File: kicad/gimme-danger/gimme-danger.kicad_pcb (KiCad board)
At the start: 4 copper layers, 46.1 x 30 mm, 74 parts, among them J3 Screw_Terminal_01x06, Q1 AO3400A, Q2 AO3400A, Q3 AO3400A, Q4 AO3400A, U1 ESP32-S3-WROOM-1, U2 TPD6S300RUKR, U3 U261-241N-4BS2SS, U4 AO4407A, U5 SKRKAEE020, U6 DDTC143EUA, U7 SKRKAEE020, U8 TPS54302

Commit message: v0.0.2a routing v0
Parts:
- removed C13: 0.1u, Capacitor_SMD:C_0402_1005Metric
- removed R1, R7: 10k, Resistor_SMD:R_0402_1005Metric
- removed R16: 1k, Resistor_SMD:R_0402_1005Metric
- removed R8: 100k, Resistor_SMD:R_0402_1005Metric
- removed U6: DDTC143EUA, footprint:SOT-323-3_L2.0-W1.3-P1.30-LS2.1-BR
- removed kibuzzard-65EACF24: G***, kibuzzard-65EACF24
- removed kibuzzard-65EACF30: G***, kibuzzard-65EACF30
- removed kibuzzard-65EACF3E: G***, kibuzzard-65EACF3E
- removed kibuzzard-65EACF4F: G***, kibuzzard-65EACF4F
- removed kibuzzard-65EACFAE: G***, kibuzzard-65EACFAE
- removed kibuzzard-65EAD047: G***, kibuzzard-65EAD047
- removed kibuzzard-65EAD056: G***, kibuzzard-65EAD056
- removed kibuzzard-65EAD068: G***, kibuzzard-65EAD068
- removed kibuzzard-65EAD078: G***, kibuzzard-65EAD078
- removed kibuzzard-65EAD09E: G***, kibuzzard-65EAD09E
- removed kibuzzard-65EAD0AB: G***, kibuzzard-65EAD0AB
- removed kibuzzard-65EADF23: G***, kibuzzard-65EADF23
- removed kibuzzard-65EADF47: G***, kibuzzard-65EADF47
- removed kibuzzard-65EB0655: G***, kibuzzard-65EB0655
- added C11: 220p, Capacitor_SMD:C_0402_1005Metric, F.Cu at (67.3, 120.2)
- added D4: 18V, footprint:SOD-523_L1.2-W0.8-LS1.6-RD, F.Cu at (70.4, 102.1)
- added D5: SMAJ28A, footprint:SMA_L4.3-W2.6-LS5.2-RD, F.Cu at (73.0, 64.0)
- added D6: SMAJ48A, footprint:SMA_L4.3-W2.5-LS5.0-RD, F.Cu at (94.1, 106.9)
- added D7: SMAJ28A, footprint:SMA_L4.3-W2.6-LS5.2-RD, F.Cu at (73.0, 68.0)
- added D8: SMAJ28A, footprint:SMA_L4.3-W2.6-LS5.2-RD, F.Cu at (73.0, 72.0)
- added H1: MountingHole, MountingHole:MountingHole_2.2mm_M2_Pad_Via, F.Cu at (62.5, 129.9)
- added H2: MountingHole, MountingHole:MountingHole_2.2mm_M2_Pad_Via, F.Cu at (89.2, 102.9)
- added H3: MountingHole, MountingHole:MountingHole_2.2mm_M2_Pad_Via, F.Cu at (62.2, 93.9)
- added R22: 33k, Resistor_SMD:R_0402_1005Metric, F.Cu at (68.2, 102.1)
- added R23: 3.3k, Resistor_SMD:R_0402_1005Metric, F.Cu at (71.5, 102.4)
- added R24: 10m, footprint:R2512, F.Cu at (70.4, 98.5)
- added REF1: DMP6023LE-13, footprint:SOT-223-4_L6.5-W3.5-P2.30-LS7.0-BR, F.Cu at (70.5, 107.7)
- added REF2: DMP6023LE-13, footprint:SOT-223-4_L6.5-W3.5-P2.30-LS7.0-BR, F.Cu at (64.2, 102.0)
- added TP10: 3v3, TestPoint:TestPoint_Pad_D1.0mm, F.Cu at (84.9, 113.0)
- added TP6: 3v3, TestPoint:TestPoint_Pad_D1.0mm, B.Cu at (63.5, 123.6)
- added TP7: 3v3, TestPoint:TestPoint_Pad_D1.0mm, F.Cu at (61.0, 123.6)
- added TP8: 3v3, TestPoint:TestPoint_Pad_D1.0mm, F.Cu at (63.5, 123.6)
- added TP9: 3v3, TestPoint:TestPoint_Pad_D1.0mm, F.Cu at (66.0, 123.6)
- added U11: DDTC143EUA, footprint:SOT-323-3_L2.0-W1.3-P1.30-LS2.1-BR, F.Cu at (74.2, 102.1)
- added U9: INA219AIDR, footprint:SOIC-8_L4.9-W3.9-P1.27-LS6.0-BL, F.Cu at (81.6, 98.5)
- added kibuzzard-660041C0: G***, kibuzzard-660041C0, B.Cu at (94.0, 131.7)
- added kibuzzard-660041C6: G***, kibuzzard-660041C6, B.Cu at (91.4, 131.7)
- added kibuzzard-660041D1: G***, kibuzzard-660041D1, B.Cu at (96.5, 131.7)
- added kibuzzard-6600448B: G***, kibuzzard-6600448B, F.Cu at (61.2, 125.8)
- added kibuzzard-660044A5: G***, kibuzzard-660044A5, F.Cu at (63.7, 125.8)
- added kibuzzard-660044B0: G***, kibuzzard-660044B0, F.Cu at (66.3, 125.8)
- added kibuzzard-660044E2: G***, kibuzzard-660044E2, F.Cu at (81.9, 124.1)
- added kibuzzard-660044E7: G***, kibuzzard-660044E7, F.Cu at (85.9, 124.1)
- added kibuzzard-660044F8: G***, kibuzzard-660044F8, B.Cu at (66.0, 120.7)
- added kibuzzard-660044FF: G***, kibuzzard-660044FF, B.Cu at (66.0, 123.1)
- added kibuzzard-6600450E: G***, kibuzzard-6600450E, B.Cu at (97.4, 104.8)
- added kibuzzard-66004518: G***, kibuzzard-66004518, B.Cu at (97.2, 109.8)
- added kibuzzard-66004529: G***, kibuzzard-66004529, B.Cu at (96.4, 114.6)
- added kibuzzard-66004537: G***, kibuzzard-66004537, B.Cu at (96.5, 119.6)
- added kibuzzard-6600453E: G***, kibuzzard-6600453E, B.Cu at (96.5, 124.7)
- added kibuzzard-66004547: G***, kibuzzard-66004547, B.Cu at (96.5, 127.7)
- added kibuzzard-6600454F: G***, kibuzzard-6600454F, B.Cu at (91.2, 97.0)
- added kibuzzard-66004555: G***, kibuzzard-66004555, B.Cu at (96.1, 94.3)
- added kibuzzard-6600455C: G***, kibuzzard-6600455C, B.Cu at (101.5, 96.9)
- added kibuzzard-66004606: G***, kibuzzard-66004606, F.Cu at (87.7, 114.6)
- added kibuzzard-66004622: G***, kibuzzard-66004622, F.Cu at (87.5, 112.2)
- added kibuzzard-66004888: G***, kibuzzard-66004888, B.Cu at (78.5, 93.5)
- C1: value 0.1u -> 1u; footprint Capacitor_SMD:C_0402_1005Metric -> Capacitor_SMD:C_0603_1608Metric
- C10, C9: value 1u -> 0.1u
- C4: footprint Capacitor_SMD:C_0603_1608Metric -> Capacitor_SMD:C_0805_2012Metric
- C6: value 22n -> 22u; footprint Capacitor_SMD:C_0402_1005Metric -> Capacitor_SMD:C_0805_2012Metric
- D1, D2: footprint LED_SMD:LED_0603_1608Metric -> LED_SMD:LED_0805_2012Metric
- D3: value 1N5819WS -> SMAJ28A; footprint Diode_SMD:D_SOD-323 -> footprint:SMA_L4.3-W2.6-LS5.2-RD
- L2: value YNR6045-470M -> 47uH
- TP1: moved to F.Cu
- U2: value TPD6S300RUKR -> TYPE-C-31-M-12; footprint footprint:WQFN-20_L3.0-W3.0-P0.40-BL-EP1.7 -> footprint:USB-C_SMD-TYPE-C-31-M-12
- U3: value U261-241N-4BS2SS -> TPD4E1U06DCKR; footprint footprint:USB-C-SMD_U261-241N-4BS2SS -> footprint:SC-70-6_L2.2-W1.3-P0.65-LS2.1-BL
- U4: value AO4407A -> DC-84; footprint footprint:SOIC-8_L4.9-W3.9-P1.27-LS6.0-BL -> footprint:DC-IN-TH_DC-84
- moved U4 31.1 mm to (96.3, 94.6), turned to 90 degrees
- moved TP2 25.8 mm to (91.4, 129.8)
- moved TP3 25.8 mm to (94.0, 129.8)
- moved TP4 25.8 mm to (96.5, 129.8)
- moved C1 24.5 mm to (67.9, 95.5), turned to 0 degrees
- moved R3 23.5 mm to (86.4, 96.6)
- moved R2 21.4 mm to (86.4, 97.9)
- moved D3 19.2 mm to (88.3, 88.6)
- moved C9 18.4 mm to (69.3, 102.1), turned to -90 degrees
- moved C10 17.0 mm to (67.3, 119.2), turned to 0 degrees
- moved TP1 11.5 mm to (84.9, 115.5), turned to 0 degrees
- moved kibuzzard-65EB08B9 8.63 mm to (77.5, 122.3), turned to 0 degrees
- moved U2 7.56 mm to (63.3, 112.0)
- moved kibuzzard-65EB08A1 7.44 mm to (75.5, 122.3), turned to 0 degrees
- moved C15 7.32 mm to (80.0, 111.9), turned to 90 degrees
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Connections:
- C1 pad 1: Net-(U2-VBIAS) -> VSh+
- C10 pad 1: VOUT -> GND
- C10 pad 2: GND -> +3V3
- C14 pad 1: +3V3 -> Net-(U8-SW)
- C9 pad 1: +3V3 -> Net-(D4-A)
- C9 pad 2: GND -> Net-(D4-K)
- D3 pad 2: OUT1 -> OUT3
- KEY1 pad 1: unconnected-(KEY1-CC2-Pad1) -> CC2
- KEY1 pad 14: unconnected-(KEY1-CC2-Pad14) -> CC2
- TP5 pad 1: C_CC1 -> CC1
- U1 pad 38: VMON -> unconnected-(U1-GPIO2/TOUCH2/ADC1_CH1-Pad38)
- U2 pad 1: C_SBU1 -> (no net)
- U2 pad 2: unconnected-(U2-C_SBU2-Pad2) -> (no net)
- U2 pad 3: Net-(U2-VBIAS) -> (no net)
- U4 pad 1: VBUS -> VOUT
- U4 pad 2: VBUS -> GND
- U4 pad 3: VBUS -> GND
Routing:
- net SDA: track 12.1 -> 49.8 mm, vias 2 -> 6
- net GND: track 37.6 -> 0.00 mm, vias 15 -> 8
- net SCL: track 23.7 -> 50.4 mm, vias 2 -> 6
- net CC1: track 4.17 -> 28.8 mm, vias 0 -> 3
- net CC2: track 0.00 -> 22.8 mm, vias 0 -> 3
- net VSh+: track 0.00 -> 21.4 mm, vias 0 -> 2
- net VBUS: track 31.0 -> 11.6 mm, vias 2 -> 7
- net Net-(D4-A): track 0.00 -> 15.8 mm, vias 0 -> 2
- net LED_GREEN: track 4.87 -> 19.7 mm, vias 1 -> 2
- net TX: track 24.1 -> 10.4 mm, vias 2 -> 0
- net Net-(U1-GPIO21): track 14.9 -> 27.9 mm
- net Net-(U1-GPIO47/SPICLK_P/SUBSPICLK_P_DIFF): track 11.5 -> 24.4 mm, vias 2 -> 3
- net C_SBU1: track 12.3 -> 0.00 mm, vias 2 -> 0
- net RX: track 24.1 -> 12.6 mm, vias 2 -> 0
- net LED_RED: track 5.05 -> 15.7 mm, vias 1 -> 2
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- added copper zone on F.Cu, net Net-(D4-K)
- added copper zone on In2.Cu, net VBUS
- added copper zone on F.Cu, net VSh+
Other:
- board size 46.1 x 30 mm -> 47.7 x 42.6 mm
- board text added: "rbaron.net"

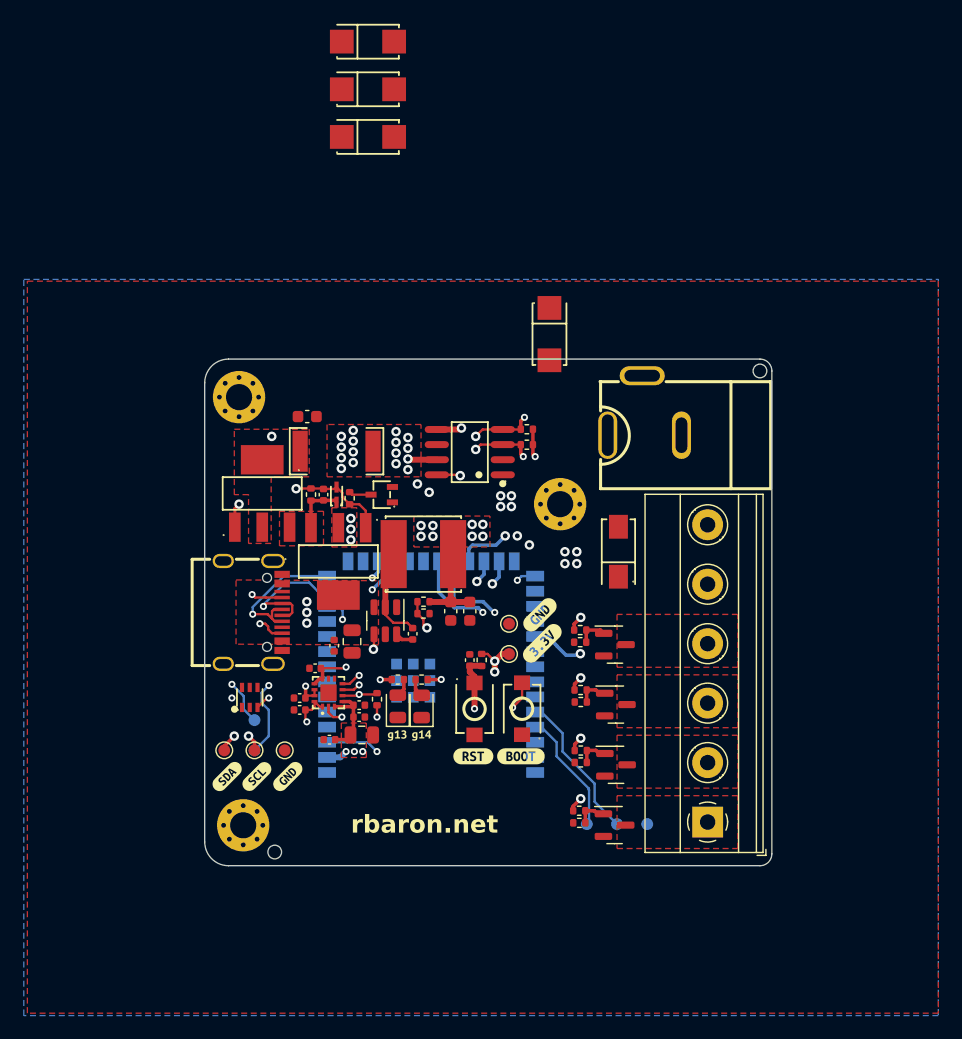
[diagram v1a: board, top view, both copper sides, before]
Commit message: Board outline is round number of mms
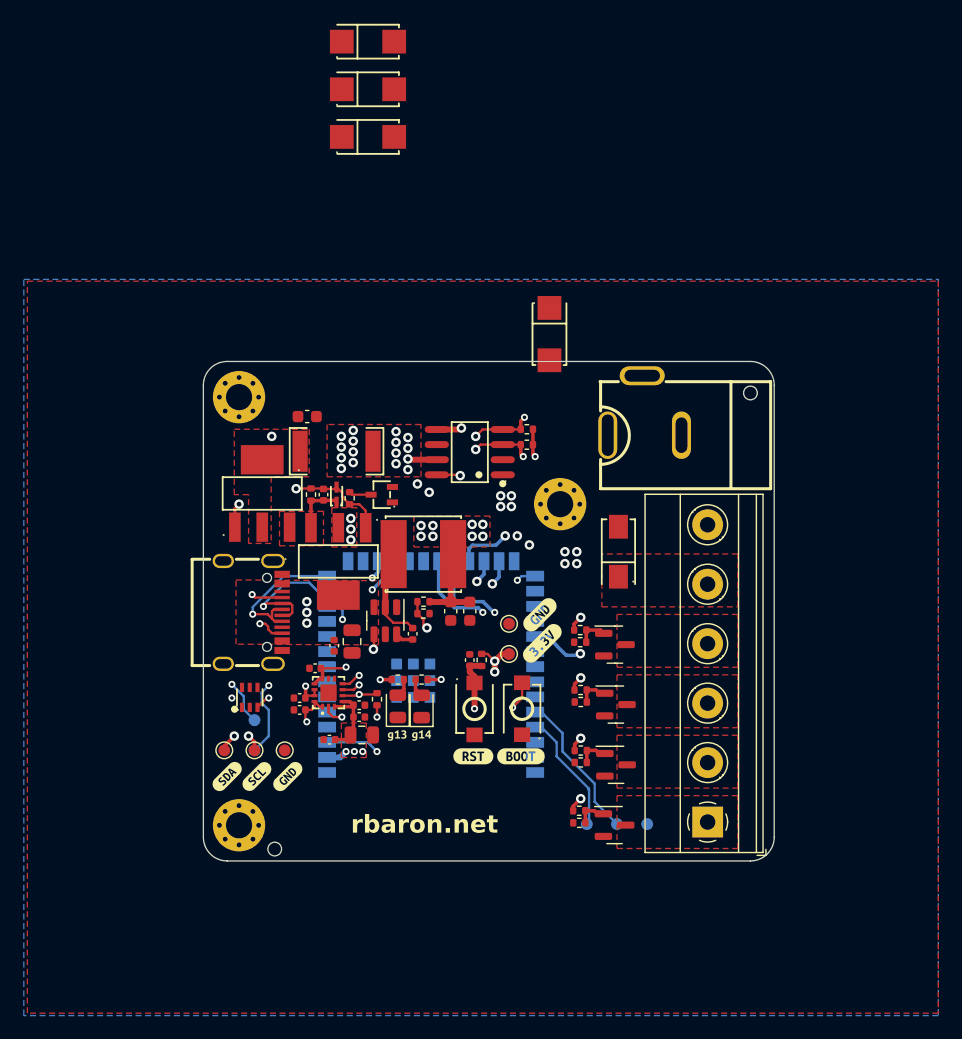
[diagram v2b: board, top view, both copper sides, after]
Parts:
- moved H1 0.35 mm to (62.2, 129.9)
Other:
- board size 47.7 x 42.6 mm -> 48 x 42 mm
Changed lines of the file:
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@@
   )
   (footprint "MountingHole:MountingHole_2.2mm_M2_Pad_Via" (layer "F.Cu")
-    (at 62.55 129.9)
+    (at 62.2 129.9)
     (descr "Mounting Hole 2.2mm, M2")
     (tags "mounting hole 2.2mm m2")
@@
       (stroke (width 0) (type solid)) (fill solid) (layer "B.SilkS"))
   )
-  (gr_circle (center 65.2 132.15) (end 65.85 132.15)
+  (gr_circle (center 65.2 131.9) (end 65.85 131.9)
     (stroke (width 0.1) (type default)) (fill none) (layer "F.Mask"))
-  (gr_circle (center 106 91.7) (end 106.65 91.7)
+  (gr_circle (center 105.2 93.55) (end 105.85 93.55)
     (stroke (width 0.1) (type default)) (fill none) (layer "F.Mask"))
-  (gr_line (start 61.314214 90.7) (end 106 90.7)
+  (gr_line (start 107.2 130.9) (end 107.2 92.9)
     (stroke (width 0.1) (type default)) (layer "Edge.Cuts"))
-  (gr_arc (start 59.314214 92.7) (mid 59.9 91.285786) (end 61.314214 90.7)
+  (gr_line (start 105.2 90.9) (end 61.2 90.9)
     (stroke (width 0.1) (type default)) (layer "Edge.Cuts"))
-  (gr_arc (start 61.314214 133.3) (mid 59.9 132.714214) (end 59.314214 131.3)
+  (gr_line (start 61.2 132.9) (end 105.2 132.9)
     (stroke (width 0.1) (type default)) (layer "Edge.Cuts"))
-  (gr_circle (center 65.2 132.15) (end 65.776 132.15)
+  (gr_circle (center 65.2 131.9) (end 65.776 131.9)
     (stroke (width 0.1) (type default)) (fill none) (layer "Edge.Cuts"))
-  (gr_line (start 59.314214 131.3) (end 59.314214 92.7)
-    (stroke (width 0.1) (type default)) (layer "Edge.Cuts"))
-  (gr_circle (center 106 91.7) (end 106.576 91.7)
+  (gr_circle (center 105.2 93.55) (end 105.776 93.55)
     (stroke (width 0.1) (type default)) (fill none) (layer "Edge.Cuts"))
-  (gr_line (start 107 91.7) (end 107 132.3)
+  (gr_arc (start 107.2 130.9) (mid 106.614214 132.314214) (end 105.2 132.9)
+    (stroke (width 0.1) (type default)) (layer "Edge.Cuts"))
+  (gr_arc (start 105.2 90.9) (mid 106.614214 91.485786) (end 107.2 92.9)
     (stroke (width 0.1) (type default)) (layer "Edge.Cuts"))
-  (gr_arc (start 107 132.3) (mid 106.707107 133.007107) (end 106 133.3)
+  (gr_line (start 59.2 92.9) (end 59.2 130.9)
     (stroke (width 0.1) (type default)) (layer "Edge.Cuts"))
-  (gr_line (start 61.314214 133.3) (end 106 133.3)
+  (gr_arc (start 59.2 92.9) (mid 59.785786 91.485786) (end 61.2 90.9)
     (stroke (width 0.1) (type default)) (layer "Edge.Cuts"))
-  (gr_arc (start 106 90.7) (mid 106.707107 90.992893) (end 107 91.7)
+  (gr_arc (start 61.2 132.9) (mid 59.785786 132.314214) (end 59.2 130.9)
     (stroke (width 0.1) (type default)) (layer "Edge.Cuts"))
   (gr_text "JLCJLCJLCJLC" (at 85.3 125.15 90) (layer "B.SilkS")
@@
       )
     )
+  )
+  (zone (net 52) (net_name "VOUT") (layer "F.Cu") (hatch edge 0.5)
+    (priority 12)
+    (connect_pads (clearance 0.1))
+    (min_thickness 0.25) (filled_areas_thickness no)
+    (fill yes (thermal_gap 0.5) (thermal_bridge_width 0.5))
+    (polygon
+      (pts
+        (xy 92.71 107.09)
+        (xy 92.71 111.535)
+        (xy 104.14 111.535)
+        (xy 104.14 107.09)
+      )
+    )

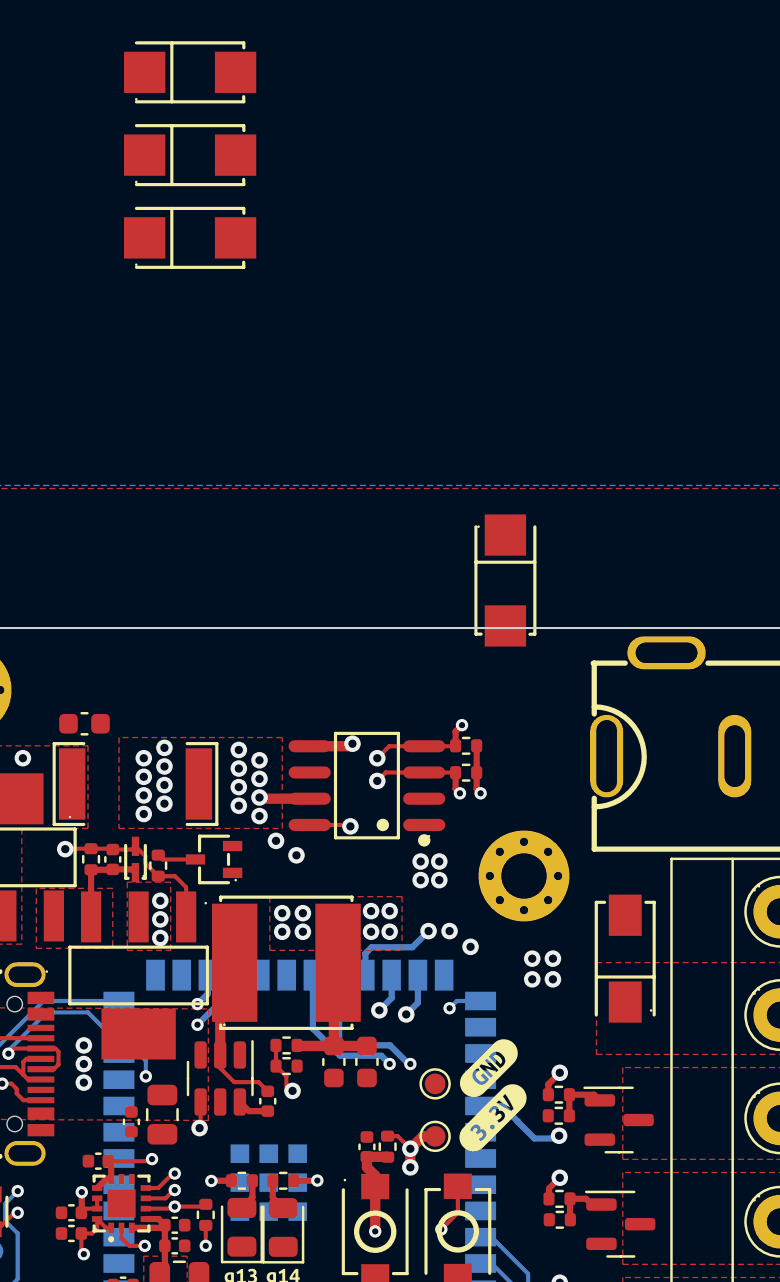
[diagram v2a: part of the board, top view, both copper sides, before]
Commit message: Add schottky on ch1
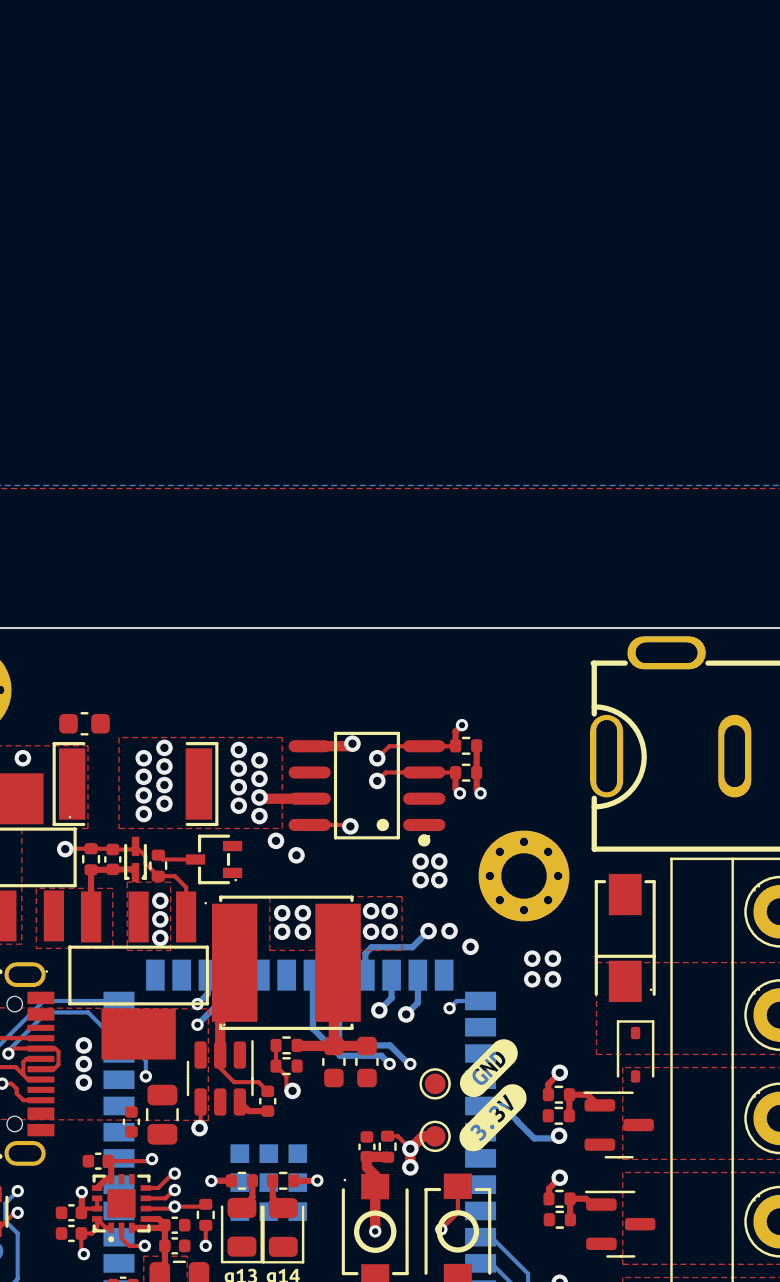
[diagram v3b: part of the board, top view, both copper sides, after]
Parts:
- removed D5, D7, D8: SMAJ28A, footprint:SMA_L4.3-W2.6-LS5.2-RD
- D3: value SMAJ28A -> 1N5819WS; footprint footprint:SMA_L4.3-W2.6-LS5.2-RD -> Diode_SMD:D_SOD-323
- moved D3 23.8 mm to (94.6, 111.5)
- moved D6 1.00 mm to (94.1, 105.9)
- moved Q1 0.24 mm to (93.8, 115.0)
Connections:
- D3 pad 2: OUT3 -> OUT1
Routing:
- net Net-(U1-GPIO38/FSPIWP/SUBSPIWP): track 19.4 -> 20.1 mm
